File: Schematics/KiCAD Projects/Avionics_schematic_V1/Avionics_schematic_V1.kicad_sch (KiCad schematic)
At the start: 7 parts, among them J1 SD_Card_Breakout, SW1 SW_Push

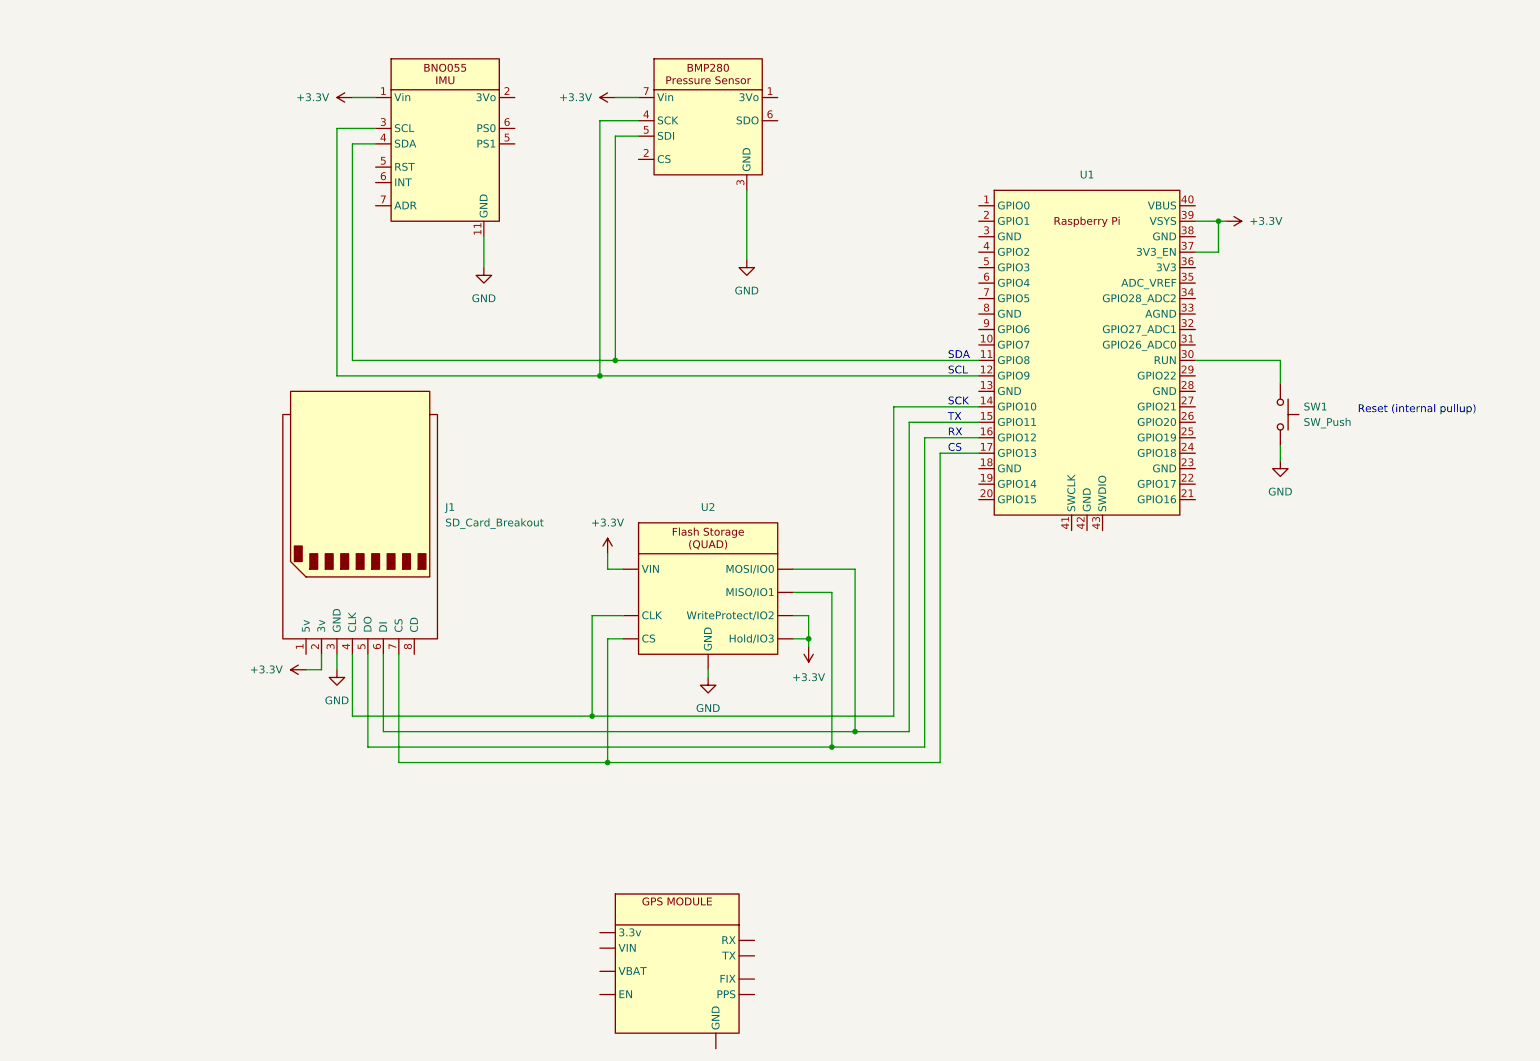
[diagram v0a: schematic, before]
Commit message: Added and implemented MAX-M10S GPS module
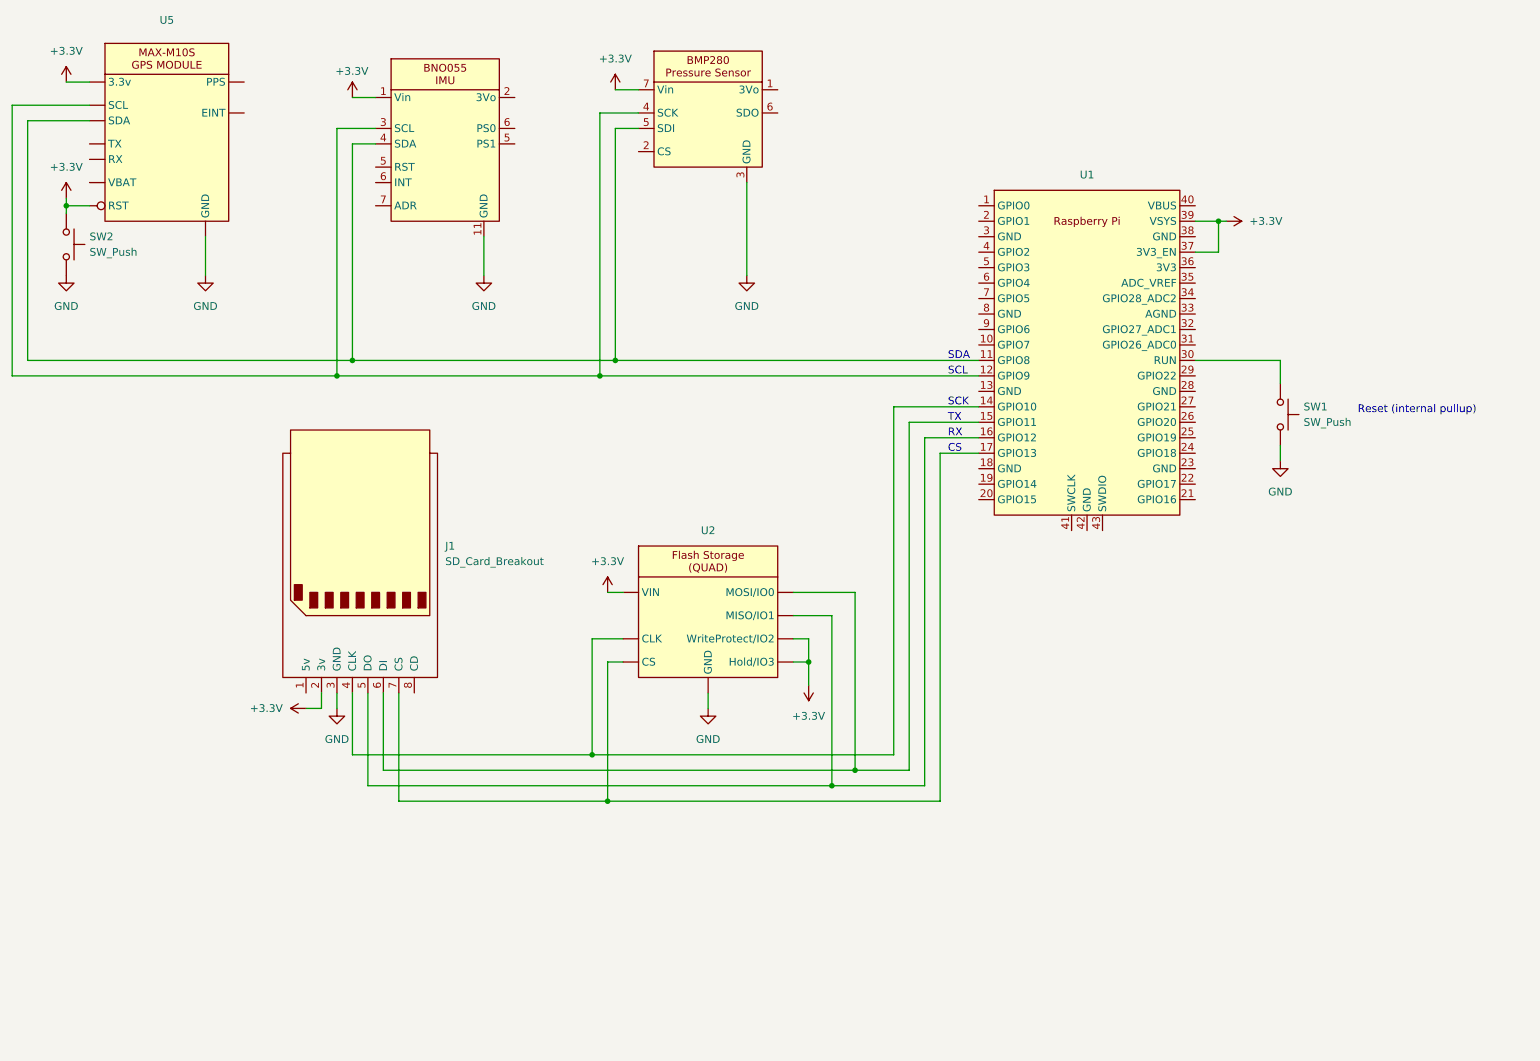
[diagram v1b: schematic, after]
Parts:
- removed e: ~, symbol Breakout_boards:GPS_Module_Breakout
- added SW2: SW_Push, symbol Switch:SW_Push
- added U5: ~, symbol Breakout_boards:GPS_MAX-M10S_Breakout
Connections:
- net +3.3V: now also SW2.1, U5. (VBAT)
- net GND: now also SW2.2, U5. (VBAT)
- net at U1.11 (GPIO8), U3.5 (SDI), U4.4 (SDA): now also U5. (VBAT)
- net at U1.12 (GPIO9), U3.4 (SCK), U4.3 (SCL): now also U5. (VBAT)
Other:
- moved on the sheet: J1, U2
